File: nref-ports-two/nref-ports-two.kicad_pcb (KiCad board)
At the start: 4 copper layers, 87.5 x 40.2 mm, 117 parts, among them J1 USB_C_Receptacle, J2 USB_C_Receptacle, J3 USB3_A, J4 HD0919MSMTTR, J5 Conn_01x20, J6 Conn_01x12_Pin, J7 Conn_01x04, U1 TUSB8041, U10 TPD4E02B04DQA, U11 TPD12S521, U12 LM2830XQMFE/NOPB, U13 LM2830XQMFE/NOPB, U2 HD3SS3220IRNHT, U3 TPD4E02B04DQA, U4 TPD4E02B04DQA, U5 TPD4E02B04DQA, U6 TPD4E02B04DQA, U7 TPD4E02B04DQA, U8 TPD4E02B04DQA, U9 TPD4E02B04DQA, Y1 24MHz

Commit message: WIP ports-two redesign
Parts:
- removed D2, D3: PMEG1020EA,115, Diode_SMD:D_SOD-323
- removed FB1, FB2: 220@100MHz 1.4A, Inductor_SMD:L_0603_1608Metric
- removed J7: Conn_01x04, Connector_JST:JST_SH_SM04B-SRSS-TB_1x04-1MP_P1.00mm_Horizontal
- removed R39, R40, R43, R44: 22k, Resistor_SMD:R_0402_1005Metric
- added C44: 0.1uF, Capacitor_SMD:C_0402_1005Metric, F.Cu at (139.2, 97.3)
- added C45: 0.1uF, Capacitor_SMD:C_0402_1005Metric, F.Cu at (132.8, 99.2)
- added C46: 0.1uF, Capacitor_SMD:C_0402_1005Metric, F.Cu at (170.3, 110.0)
- added C47: 0.1uF, Capacitor_SMD:C_0402_1005Metric, F.Cu at (170.3, 109.0)
- added C48: 1uF, Capacitor_SMD:C_0402_1005Metric, F.Cu at (180.2, 104.3)
- added C49: 1uF, Capacitor_SMD:C_0402_1005Metric, F.Cu at (182.5, 104.3)
- added C50: 4.7uF, Capacitor_SMD:C_0402_1005Metric, F.Cu at (173.3, 110.1)
- added C51: 4.7uF, Capacitor_SMD:C_0402_1005Metric, F.Cu at (176.8, 103.8)
- added C52: 0.1uF, Capacitor_SMD:C_0402_1005Metric, F.Cu at (173.3, 112.0)
- added C53: 1uF, Capacitor_SMD:C_0402_1005Metric, F.Cu at (173.3, 111.0)
- added C54: 1uF, Capacitor_SMD:C_0402_1005Metric, F.Cu at (179.7, 106.0)
- added C55: 0.1uF, Capacitor_SMD:C_0402_1005Metric, F.Cu at (178.7, 106.0)
- added C56: 0.1uF, Capacitor_SMD:C_0402_1005Metric, F.Cu at (172.6, 103.8)
- added C57: 0.1uF, Capacitor_SMD:C_0402_1005Metric, F.Cu at (172.6, 102.9)
- added C58: 0.1uF, Capacitor_SMD:C_0402_1005Metric, F.Cu at (175.8, 111.2)
- added C59: 0.1uF, Capacitor_SMD:C_0402_1005Metric, F.Cu at (174.8, 111.2)
- added FB5: 100@100MHz 3A, Inductor_SMD:L_0402_1005Metric, F.Cu at (171.9, 111.0)
- added FB6: 100@100MHz 3A, Inductor_SMD:L_0402_1005Metric, F.Cu at (176.8, 102.8)
- added J8: Conn_01x12_Pin, Connector_FFC-FPC:Hirose_FH12-12S-0.5SH_1x12-1MP_P0.50mm_Horizontal, F.Cu at (149.7, 115.5)
- added R10: 0, Resistor_SMD:R_0402_1005Metric, F.Cu at (178.2, 104.0)
- added R19: 900k, Resistor_SMD:R_0402_1005Metric, F.Cu at (132.9, 104.3)
- added R20: 0, Resistor_SMD:R_0402_1005Metric, F.Cu at (172.2, 97.2)
- added TP3: TestPoint, TestPoint:TestPoint_Pad_D1.0mm, F.Cu at (129.6, 102.0)
- added TP4: TestPoint, TestPoint:TestPoint_Pad_D1.0mm, F.Cu at (181.5, 99.0)
- added TP5: TestPoint, TestPoint:TestPoint_Pad_D1.0mm, F.Cu at (185.9, 100.0)
- added TP6: TestPoint, TestPoint:TestPoint_Pad_D1.0mm, F.Cu at (185.2, 98.0)
- added TP7: TestPoint, TestPoint:TestPoint_Pad_D1.0mm, F.Cu at (129.6, 99.9)
- added U14: EQCO5X31C0-I_6NX, footprints:QFN50P400X400X100-21N-D, F.Cu at (175.1, 107.0)
- added U15: LP5907MFX-1.2, Package_TO_SOT_SMD:SOT-23-5, F.Cu at (181.3, 102.2)
- added U16: TUSB321, Package_DFN_QFN:Texas_X2QFN-12_1.6x1.6mm_P0.4mm, F.Cu at (183.6, 93.9)
- added U17: TMUXHS4212, footprints:Texas-VQFN20_2.5x4.5mm_RKS, F.Cu at (136.1, 95.7)
- added U18: TUSB321, Package_DFN_QFN:Texas_X2QFN-12_1.6x1.6mm_P0.4mm, F.Cu at (133.3, 101.1)
- C17: value 47uF -> 0.1uF; footprint Capacitor_SMD:C_1206_3216Metric -> Capacitor_SMD:C_0402_1005Metric
- J1, J2: footprint footprints:MOLEX_105450-0101 -> Connector_USB:USB_C_Receptacle_Molex_105450-0101
- J5: footprint Connector_FFC-FPC:Hirose_FH12-20S-0.5SH_1x20-1MP_P0.50mm_Horizontal -> footprints:AMPHENOL_SFV20R-2STE1HLF
- R11: value 10k -> 0
- R12: value 900k -> 10k
- R13, R22: value 200k -> 10k
- R14: value 0 -> 4.7k
- R15: value 0 -> 900k
- R18, R24: value 200k -> 0
- R23: value 200k -> 4.7k
- R31, R35, R36: value 100k -> 10k
- TP1, TP2: footprint TestPoint:TestPoint_Pad_1.0x1.0mm -> TestPoint:TestPoint_Pad_D1.0mm
- U12, U13: value LM2830XQMFE/NOPB -> TLV62569DBV
- U2: value HD3SS3220IRNHT -> TMUXHS4212; footprint footprints:QFN40P450X250X80-31N120X320 -> footprints:Texas-VQFN20_2.5x4.5mm_RKS
- moved TP2 65.5 mm to (193.4, 100.1)
- moved TP1 64.0 mm to (192.6, 89.8)
- moved R14 54.3 mm to (183.5, 97.0), turned to 0 degrees
- moved C17 53.6 mm to (179.9, 99.3), turned to 0 degrees
- moved R15 53.4 mm to (183.5, 98.0), turned to 0 degrees
- moved R13 53.2 mm to (183.5, 96.1), turned to 0 degrees
- moved R12 52.2 mm to (183.9, 102.5), turned to -90 degrees
- moved R21 49.7 mm to (185.5, 93.4)
- moved C18 48.4 mm to (183.1, 92.0), turned to 0 degrees
- moved U2 43.9 mm to (176.9, 97.1)
- moved R25 43.6 mm to (166.8, 117.8), turned to 180 degrees
- moved R24 41.4 mm to (164.6, 117.8), turned to 0 degrees
- moved C21 28.9 mm to (180.3, 94.0)
- moved C23 28.8 mm to (181.3, 94.0)
- moved C22 28.2 mm to (172.8, 94.0)
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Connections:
- net /USB3_1_SSTXCN renamed /USBH3_TXCN
- net /USB3_1_SSTXCP renamed /USBH3_TXCP
- net /USBH_1A_AC_TXN renamed /USBC2A_TXCN
- net /USBH_1A_AC_TXP renamed /USBC2A_TXCP
- net /USBH_1B_AC_TXN renamed /USBC2B_TXCN
- net /USBH_1B_AC_TXP renamed /USBC2B_TXCP
- net /USBH_2A_AC_TXN renamed /USBC1A_TXCN
- net /USBH_2A_AC_TXP renamed /USBC1A_TXCP
- net /USBH_2B_AC_TXN renamed /USBC1B_TXCN
- net /USBH_2B_AC_TXP renamed /USBC1B_TXCP
- net CC1 renamed USBC1_CC1
- net CC2 renamed USBC1_CC2
- C17 pad 1: MUX_5V -> /MUX_3V3
- C18 pad 1: MUX_3V3 -> +5V
- C21 pad 2: USBH_2A_TXN -> USBC1A_TXN
- C22 pad 2: USBH_2B_TXN -> USBC1B_TXN
- C23 pad 2: USBH_2A_TXP -> USBC1A_TXP
- C24 pad 2: USBH_2B_TXP -> USBC1B_TXP
- C27 pad 2: USBH_MUXA_TXN -> USBC2A_TXN
- C28 pad 2: USBH_MUXB_TXN -> USBC2B_TXN
- C29 pad 2: USBH_MUXA_TXP -> USBC2A_TXP
- C30 pad 2: USBH_MUXB_TXP -> USBC2B_TXP
- C34 pad 1: USBH_1A_TXN -> USBH3_TXN
- C36 pad 1: USBH_1A_TXP -> USBH3_TXP
- J1 pad A10: USBH_2B_RXN -> USBC1B_RXN
- J1 pad A11: USBH_2B_RXP -> USBC1B_RXP
- J1 pad A6: USBH_2_DP -> USBC1_DP
- J1 pad A7: USBH_2_DN -> USBC1_DN
- J1 pad B10: USBH_2A_RXN -> USBC1A_RXN
- J1 pad B11: USBH_2A_RXP -> USBC1A_RXP
- J1 pad B6: USBH_2_DP -> USBC1_DP
- J1 pad B7: USBH_2_DN -> USBC1_DN
- J2 pad A10: USBH_MUXB_RXN -> USBC2B_RXN
- J2 pad A11: USBH_MUXB_RXP -> USBC2B_RXP
- J2 pad A5: MUXCC1 -> USBC2_CC1
- J2 pad A6: USBH_1_DP -> USBC2_DP
- J2 pad A7: USBH_1_DN -> USBC2_DN
- J2 pad B10: USBH_MUXA_RXN -> USBC2A_RXN
- J2 pad B11: USBH_MUXA_RXP -> USBC2A_RXP
- J2 pad B5: MUXCC2 -> USBC2_CC2
- J2 pad B6: USBH_1_DP -> USBC2_DP
- J2 pad B7: USBH_1_DN -> USBC2_DN
- J3 pad 5: USBH_1A_RXN -> USBH3_RXN
- J3 pad 6: USBH_1A_RXP -> USBH3_RXP
- J5 pad 1: Net-(J5-Pin_1) -> HDMI_TX2P
- J5 pad 10: HDMI_CLKN -> HDMI_CLKP
- J5 pad 11: HDMI_CLKP -> HDMI_CLKN
- J5 pad 13: HDMI_TX0N -> GND
- J5 pad 14: HDMI_TX0P -> HDMI_CEC
- J5 pad 15: GND -> HDMI_SCL
- J5 pad 16: HDMI_TX1N -> HDMI_SDA
- J5 pad 17: HDMI_TX1P -> HDMI_HPD
- J5 pad 18: GND -> Net-(J5-Pin_18)
- J5 pad 19: HDMI_TX2N -> Net-(J5-Pin_18)
- J5 pad 2: Net-(J5-Pin_1) -> HDMI_TX2N
- J5 pad 20: HDMI_TX2P -> Net-(J5-Pin_18)
- J5 pad 3: Net-(J5-Pin_1) -> GND
- J5 pad 4: HDMI_HPD -> HDMI_TX1P
- J5 pad 5: HDMI_SCL -> HDMI_TX1N
- J5 pad 6: HDMI_SDA -> GND
- J5 pad 7: HDMI_CEC -> HDMI_TX0P
- J5 pad 8: GND -> HDMI_TX0N
- L1 pad 1: Net-(D2-K) -> Net-(U12-SW)
- L2 pad 1: Net-(D3-K) -> Net-(U13-SW)
- R1 pad 1: Net-(J5-Pin_1) -> Net-(J5-Pin_18)
- R11 pad 1: MUX_5V -> /MUX_3V3
- R11 pad 2: Net-(U2-CURRENT_MODE) -> +3V3
- R12 pad 1: MUX_5V -> Net-(U15-EN)
- R12 pad 2: Net-(U2-VBUS_DET) -> +3V3
- R13 pad 1: MUX_5V -> +5V
- R13 pad 2: Net-(U2-PORT) -> Net-(U16-CURRENT_MODE)
- R14 pad 1: MUXCC2 -> +5V
- R14 pad 2: Net-(U2-CC2) -> Net-(U16-PORT)
- R15 pad 1: MUXCC1 -> +5V
- R15 pad 2: Net-(U2-CC1) -> Net-(U16-VBUS_DET)
- R16 pad 1: GND -> /MUX_3V3
- R16 pad 2: Net-(U2-~{ENN_CC}) -> +3V3
- R17 pad 1: GND -> ~{USB_MUX_OE}
- R17 pad 2: Net-(U2-~{ENN_MUX}) -> Net-(U17-~{OE})
- R18 pad 1: Net-(U2-DIR) -> USBC2_MUX_DIR
- R18 pad 2: MUX_3V3 -> Net-(U17-SEL)
- R21 pad 1: MUX_3V3 -> USBC1_MUX_DIR
- R21 pad 2: +3V3 -> Net-(U2-SEL)
- R22 pad 1: Net-(U2-ID) -> +5V
- R22 pad 2: MUX_5V -> Net-(U18-CURRENT_MODE)
- R23 pad 1: Net-(U2-~{INT_N}/OUT3) -> +5V
- R23 pad 2: MUX_5V -> Net-(U18-PORT)
- R24 pad 1: Net-(U2-VCONN_FAULT_N) -> +3V3
- R24 pad 2: MUX_5V -> USBH_3V3
- R25 pad 1: MUX_5V -> +1V1
- R25 pad 2: +5V -> USBH_1V1
- TP1 pad 1: Net-(U2-SCL/OUT2) -> Net-(U16-ID)
- TP2 pad 1: Net-(U2-SDA/OUT1) -> Net-(U16-~{VCONN_FAULT})
- U1 pad 1: USBH_1_DP -> USBC1_DP
- U1 pad 10: USBH_2_DN -> USBH_3_DN
- U1 pad 11: USBH_2A_TXP -> USBH3_TXP
- U1 pad 12: USBH_2A_TXN -> USBH3_TXN
- U1 pad 14: USBH_2A_RXP -> USBH3_RXP
- U1 pad 15: USBH_2A_RXN -> USBH3_RXN
- U1 pad 17: USBH_3_DP -> USBC2_DP
- U1 pad 18: USBH_3_DN -> USBC2_DN
- U1 pad 19: USBH_2B_TXP -> USBH2_TXP
- U1 pad 2: USBH_1_DN -> USBC1_DN
- U1 pad 20: USBH_2B_TXN -> USBH2_TXN
- U1 pad 22: USBH_2B_RXN -> USBH2_RXP
- U1 pad 23: USBH_2B_RXP -> USBH2_RXN
- U1 pad 26: USBH_1B_TXP -> USBH4_TXN
- U1 pad 27: USBH_1B_TXN -> USBH4_TXP
- U1 pad 29: USBH_1B_RXN -> USBH4_RXN
- U1 pad 3: USBH_1A_TXP -> USBH1_TXP
- U1 pad 30: USBH_1B_RXP -> USBH4_RXP
- U1 pad 4: USBH_1A_TXN -> USBH1_TXN
- U1 pad 55: USB2_RXP -> /UP_SSTXP
- U1 pad 56: USB2_RXN -> /UP_SSTXN
- U1 pad 58: USB2_TXP -> USB2_RE_TXN
- U1 pad 59: USB2_TXN -> USB2_RE_TXP
- U1 pad 6: USBH_1A_RXP -> USBH1_RXP
- U1 pad 7: USBH_1A_RXN -> USBH1_RXN
- U1 pad 9: USBH_2_DP -> USBH_3_DP
- U12 pad 1: Net-(D2-K) -> Net-(U12-EN)
- U12 pad 3: Net-(U12-FB) -> Net-(U12-SW)
- U12 pad 4: Net-(U12-EN) -> +5V
- U12 pad 5: +5V -> Net-(U12-FB)
- U13 pad 1: Net-(D3-K) -> Net-(U13-EN)
- U13 pad 3: Net-(U13-FB) -> Net-(U13-SW)
- U13 pad 4: Net-(U13-EN) -> +5V
- U13 pad 5: +5V -> Net-(U13-FB)
- U2 pad 1: Net-(U2-CC2) -> unconnected-(U2-RSVD1-Pad1)
- U2 pad 10: USBH_1B_RXN -> unconnected-(U2-RSVD2-Pad10)
- U2 pad 11: Net-(U2-DIR) -> GND
- U2 pad 12: Net-(U2-~{ENN_MUX}) -> USBC1B_TXP
- U2 pad 13: GND -> USBC1B_TXN
- U2 pad 14: USBH_MUXA_RXN -> USBC1B_RXP
- U2 pad 15: USBH_MUXA_RXP -> USBC1B_RXN
- U2 pad 16: USBH_MUXA_TXN -> USBC1A_TXN
- U2 pad 17: USBH_MUXA_TXP -> USBC1A_TXP
- U2 pad 18: USBH_MUXB_RXN -> USBC1A_RXN
- U2 pad 19: USBH_MUXB_RXP -> USBC1A_RXP
- U2 pad 2: Net-(U2-CC1) -> Net-(U2-~{OE})
- U2 pad 20: USBH_MUXB_TXN -> GND
- U2 pad 3: Net-(U2-CURRENT_MODE) -> USBH1_RXN
- U2 pad 4: Net-(U2-PORT) -> USBH1_RXP
- U2 pad 5: Net-(U2-VBUS_DET) -> GND
- U2 pad 6: USBH_1B_TXP -> /MUX_3V3
- U2 pad 7: USBH_1B_TXN -> USBH1_TXN
- U2 pad 8: MUX_3V3 -> USBH1_TXP
- U2 pad 9: USBH_1B_RXP -> Net-(U2-SEL)
- U3 pad 4: USBH_2_DN -> USBC1_DN
- U3 pad 5: USBH_2_DP -> USBC1_DP
- U3 pad 6: USBH_2_DP -> USBC1_DP
- U3 pad 7: USBH_2_DN -> USBC1_DN
- U4 pad 1: USBH_2A_RXN -> USBC1A_RXN
- U4 pad 10: USBH_2A_RXN -> USBC1A_RXN
- U4 pad 2: USBH_2A_RXP -> USBC1A_RXP
- U4 pad 9: USBH_2A_RXP -> USBC1A_RXP
- U5 pad 1: USBH_2B_RXN -> USBC1B_RXN
- U5 pad 10: USBH_2B_RXN -> USBC1B_RXN
- U5 pad 2: USBH_2B_RXP -> USBC1B_RXP
- U5 pad 9: USBH_2B_RXP -> USBC1B_RXP
- U6 pad 1: MUXCC1 -> USBC2_CC1
- U6 pad 10: MUXCC1 -> USBC2_CC1
- U6 pad 2: MUXCC2 -> USBC2_CC2
- U6 pad 4: USBH_1_DN -> USBC2_DN
- U6 pad 5: USBH_1_DP -> USBC2_DP
- U6 pad 6: USBH_1_DP -> USBC2_DP
- U6 pad 7: USBH_1_DN -> USBC2_DN
- U6 pad 9: MUXCC2 -> USBC2_CC2
- U7 pad 1: USBH_MUXA_RXN -> USBC2A_RXN
- U7 pad 10: USBH_MUXA_RXN -> USBC2A_RXN
- U7 pad 2: USBH_MUXA_RXP -> USBC2A_RXP
- U7 pad 9: USBH_MUXA_RXP -> USBC2A_RXP
- U8 pad 1: USBH_MUXB_RXN -> USBC2B_RXN
- U8 pad 10: USBH_MUXB_RXN -> USBC2B_RXN
- U8 pad 2: USBH_MUXB_RXP -> USBC2B_RXP
- U8 pad 9: USBH_MUXB_RXP -> USBC2B_RXP
- U9 pad 1: USBH_3_DN -> USBH_3_DP
- U9 pad 10: USBH_3_DN -> USBH_3_DP
- U9 pad 2: USBH_3_DP -> USBH_3_DN
- U9 pad 4: USBH_1A_RXP -> USBH3_RXP
- U9 pad 5: USBH_1A_RXN -> USBH3_RXN
- U9 pad 6: USBH_1A_RXN -> USBH3_RXN
- U9 pad 7: USBH_1A_RXP -> USBH3_RXP
- U9 pad 9: USBH_3_DP -> USBH_3_DN
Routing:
- net +5V: track 256.6 -> 60.2 mm, vias 9 -> 3
- net USBH_1V1: track 113.2 -> 7.58 mm, vias 12 -> 1
- net GND: track 122.1 -> 25.6 mm, vias 90 -> 22
- net USBH_3V3: track 77.4 -> 10.6 mm, vias 5 -> 0
- net USBH_1_DP: track 63.9 -> 0.00 mm, vias 4 -> 0
- net USBH_1_DN: track 63.8 -> 0.00 mm, vias 2 -> 0
- net Net-(J4-CEC): track 58.8 -> 0.00 mm, vias 1 -> 0
- net USBH_2B_RXP: track 55.8 -> 0.00 mm, vias 2 -> 0
- net USBH_2B_RXN: track 54.9 -> 0.00 mm, vias 2 -> 0
- net USBH_2A_RXN: track 52.5 -> 0.00 mm, vias 4 -> 0
- net USBH_2A_RXP: track 51.2 -> 0.00 mm, vias 4 -> 0
- net Net-(J4-SCL): track 50.3 -> 0.00 mm, vias 1 -> 0
- net USBH_2_DN: track 49.4 -> 0.00 mm, vias 4 -> 0
- net /USBC1A_TXCN: track 48.6 -> 0.79 mm, vias 2 -> 0
- net /USBC1B_TXCN: track 47.8 -> 0.00 mm, vias 2 -> 0
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
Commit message: ports-two: more routing
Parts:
- moved R11 52.9 mm to (179.6, 100.0)
- moved C11 16.9 mm to (153.0, 109.9)
- moved C14 16.6 mm to (156.9, 100.0), turned to 90 degrees
- moved C13 16.1 mm to (167.1, 108.8), turned to 0 degrees
- moved R22 10.6 mm to (128.2, 101.8), turned to 90 degrees
- moved R23 10.2 mm to (129.2, 101.8), turned to 90 degrees
- moved TP2 8.37 mm to (186.1, 96.0)
- moved R18 7.10 mm to (130.2, 96.8)
- moved TP1 7.05 mm to (185.8, 91.8)
- moved R21 6.97 mm to (180.3, 98.1), turned to 180 degrees
- moved R24 5.63 mm to (159.0, 118.5), turned to 90 degrees
- moved C45 4.89 mm to (128.2, 97.3), turned to 180 degrees
- moved R16 4.70 mm to (132.4, 107.9), turned to -90 degrees
- moved R3 4.38 mm to (162.1, 116.8), turned to 180 degrees
- moved U18 4.11 mm to (129.6, 99.3)
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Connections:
- C17 pad 1: /MUX_3V3 -> Net-(U2-VCC)
- C44 pad 1: /MUX_3V3 -> Net-(U17-VCC)
- R11 pad 1: /MUX_3V3 -> Net-(U2-VCC)
- R16 pad 1: /MUX_3V3 -> Net-(U17-VCC)
- U17 pad 12: USBC2B_TXP -> USBC2A_TXP
- U17 pad 13: USBC2B_TXN -> USBC2A_TXN
- U17 pad 14: USBC2B_RXP -> USBC2A_RXP
- U17 pad 15: USBC2B_RXN -> USBC2A_RXN
- U17 pad 16: USBC2A_TXN -> USBC2B_TXN
- U17 pad 17: USBC2A_TXP -> USBC2B_TXP
- U17 pad 18: USBC2A_RXN -> USBC2B_RXN
- U17 pad 19: USBC2A_RXP -> USBC2B_RXP
- U17 pad 6: /MUX_3V3 -> Net-(U17-VCC)
- U2 pad 12: USBC1B_TXP -> USBC1A_TXP
- U2 pad 13: USBC1B_TXN -> USBC1A_TXN
- U2 pad 14: USBC1B_RXP -> USBC1A_RXP
- U2 pad 15: USBC1B_RXN -> USBC1A_RXN
- U2 pad 16: USBC1A_TXN -> USBC1B_TXN
- U2 pad 17: USBC1A_TXP -> USBC1B_TXP
- U2 pad 18: USBC1A_RXN -> USBC1B_RXN
- U2 pad 19: USBC1A_RXP -> USBC1B_RXP
- U2 pad 6: /MUX_3V3 -> Net-(U2-VCC)
- U5 pad 1: USBC1B_RXN -> /USBC1B_TXCN
- U5 pad 10: USBC1B_RXN -> /USBC1B_TXCN
- U5 pad 2: USBC1B_RXP -> /USBC1B_TXCP
- U5 pad 4: /USBC1B_TXCP -> USBC1B_RXN
- U5 pad 5: /USBC1B_TXCN -> USBC1B_RXP
- U5 pad 6: /USBC1B_TXCN -> USBC1B_RXP
- U5 pad 7: /USBC1B_TXCP -> USBC1B_RXN
- U5 pad 9: USBC1B_RXP -> /USBC1B_TXCP
- U8 pad 1: USBC2B_RXN -> /USBC2B_TXCN
- U8 pad 10: USBC2B_RXN -> /USBC2B_TXCN
- U8 pad 2: USBC2B_RXP -> /USBC2B_TXCP
- U8 pad 4: /USBC2B_TXCN -> USBC2B_RXN
- U8 pad 5: /USBC2B_TXCP -> USBC2B_RXP
- U8 pad 6: /USBC2B_TXCP -> USBC2B_RXP
- U8 pad 7: /USBC2B_TXCN -> USBC2B_RXN
- U8 pad 9: USBC2B_RXP -> /USBC2B_TXCP
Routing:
- net +5V: track 60.2 -> 158.3 mm, vias 3 -> 16
- net USBH_1V1: track 7.58 -> 58.2 mm, vias 1 -> 8
- net USBH_3V3: track 10.6 -> 53.7 mm, vias 0 -> 4
- net GND: track 25.6 -> 63.1 mm, vias 22 -> 78
- net USBC1_DN: track 1.37 -> 27.8 mm, vias 1 -> 4
- net USBC1_DP: track 1.08 -> 27.5 mm, vias 1 -> 2
- net USBC2_CC2: track 0.00 -> 18.7 mm, vias 0 -> 4
- net USBC2_CC1: track 0.00 -> 17.2 mm, vias 0 -> 4
- net USBC1_CC2: track 0.00 -> 15.0 mm, vias 0 -> 4
- net USBC1_CC1: track 0.00 -> 14.5 mm, vias 0 -> 4
- net USBC2_DN: track 19.7 -> 32.5 mm, vias 0 -> 4
- net USBC2_DP: track 19.2 -> 31.7 mm, vias 0 -> 2
- net USBC1A_RXP: track 0.00 -> 11.4 mm, vias 0 -> 2
- net USBC2A_RXP: track 0.00 -> 11.4 mm, vias 0 -> 2
- net USBC2A_RXN: track 0.00 -> 11.3 mm, vias 0 -> 2
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
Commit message: commit various notes / polishing for ports-one and ports-two
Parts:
- added R39: 0, Resistor_SMD:R_0402_1005Metric, F.Cu at (182.9, 94.7)
- added R40: 0, Resistor_SMD:R_0402_1005Metric, F.Cu at (127.2, 98.8)
- added R43: 0, Resistor_SMD:R_0402_1005Metric, F.Cu at (127.2, 99.8)
- R15, R19: value 900k -> 909k
- R17, R20: value 0 -> 10k
- moved H3 68.4 mm to (115.3, 114.8), turned to 0 degrees
- moved R1 65.3 mm to (182.9, 93.7)
- moved C37 19.5 mm to (108.1, 108.3), turned to 180 degrees
- moved C35 18.3 mm to (108.1, 106.5), turned to 0 degrees
- moved TP4 18.0 mm to (183.7, 117.6)
- moved TP6 16.7 mm to (184.8, 115.8)
- moved C38 16.2 mm to (108.7, 100.2), turned to -90 degrees
- moved TP5 16.2 mm to (182.7, 115.8)
- moved C33 6.13 mm to (108.2, 98.8), turned to 0 degrees
- moved R28 3.80 mm to (121.7, 101.0)
- moved R16 3.79 mm to (134.2, 104.5)
- moved R26 3.59 mm to (108.1, 107.4), turned to 0 degrees
- moved TP2 3.45 mm to (186.1, 99.5)
- moved R41 1.87 mm to (140.1, 114.2), turned to 180 degrees
- moved R15 1.16 mm to (186.1, 96.8)
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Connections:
- J5 pad 18: Net-(J5-Pin_18) -> +5V
- J5 pad 19: Net-(J5-Pin_18) -> +5V
- J5 pad 20: Net-(J5-Pin_18) -> +5V
- R1 pad 1: Net-(J5-Pin_18) -> USBC1_CC1
- R1 pad 2: +5V -> Net-(U16-CC1)
- R17 pad 1: ~{USB_MUX_OE} -> Net-(U17-~{OE})
- R17 pad 2: Net-(U17-~{OE}) -> GND
- R20 pad 1: ~{USB_MUX_OE} -> GND
- U16 pad 1: USBC1_CC1 -> Net-(U16-CC1)
- U16 pad 2: USBC1_CC2 -> Net-(U16-CC2)
- U18 pad 1: USBC2_CC1 -> Net-(U18-CC1)
- U18 pad 2: USBC2_CC2 -> Net-(U18-CC2)
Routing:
- net +5V: track 158.3 -> 290.7 mm, vias 16 -> 32
- net +3V3: track 89.8 -> 154.5 mm, vias 3 -> 9
- net Net-(J4-CEC): track 0.00 -> 20.3 mm
- net Net-(J4-+5V): track 0.00 -> 18.9 mm, vias 0 -> 2
- net Net-(J4-SCL): track 0.00 -> 15.4 mm, vias 0 -> 1
- net GND: track 63.1 -> 78.1 mm, vias 78 -> 244
- net Net-(U14-TSC): track 0.50 -> 14.9 mm, vias 1 -> 2
- net Net-(J4-HPD): track 0.00 -> 13.4 mm, vias 0 -> 2
- net Net-(J4-SDA): track 0.00 -> 12.8 mm, vias 0 -> 1
- net Net-(U14-LOM): track 0.00 -> 11.8 mm, vias 0 -> 2
- net Net-(U14-TSI): track 0.00 -> 10.7 mm, vias 0 -> 2
- net Net-(U17-VCC): track 1.07 -> 7.27 mm, vias 1 -> 2
- net HDMI_TX2P: track 28.7 -> 32.1 mm
- net Net-(U16-~{VCONN_FAULT}): track 1.92 -> 5.16 mm
- net Net-(U11-LV_SUPPLY): track 0.00 -> 3.15 mm
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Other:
- board text added: "HDMI"
- board text added: "Stackup: JLC04161H-3313 90 ohms coplanar diff pairs, w: 0.1547mm, s: 0.2mm"
- board text added: "USB▶CAM"
- board text added: "USB◀MB"

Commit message: PCBs: add various notes
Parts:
- added C60: 0.1uF, Capacitor_SMD:C_0402_1005Metric, F.Cu at (171.2, 61.1)
- added C61: 0.1uF, Capacitor_SMD:C_0402_1005Metric, F.Cu at (171.2, 63.1)
- added R44: 4.7k, Resistor_SMD:R_0402_1005Metric, F.Cu at (168.3, 61.1)
- added R45: 4.7k, Resistor_SMD:R_0402_1005Metric, F.Cu at (168.3, 63.1)
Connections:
- J8 pad 4: USBH4_TXN -> /USBH4_AC_TXN
- J8 pad 5: USBH4_TXP -> /USBH4_AC_TXP
- R1 pad 1: USBC1_CC1 -> USBC1_CC2
- R39 pad 1: USBC1_CC2 -> USBC1_CC1
- R40 pad 1: USBC2_CC1 -> USBC2_CC2
- R43 pad 1: USBC2_CC2 -> USBC2_CC1

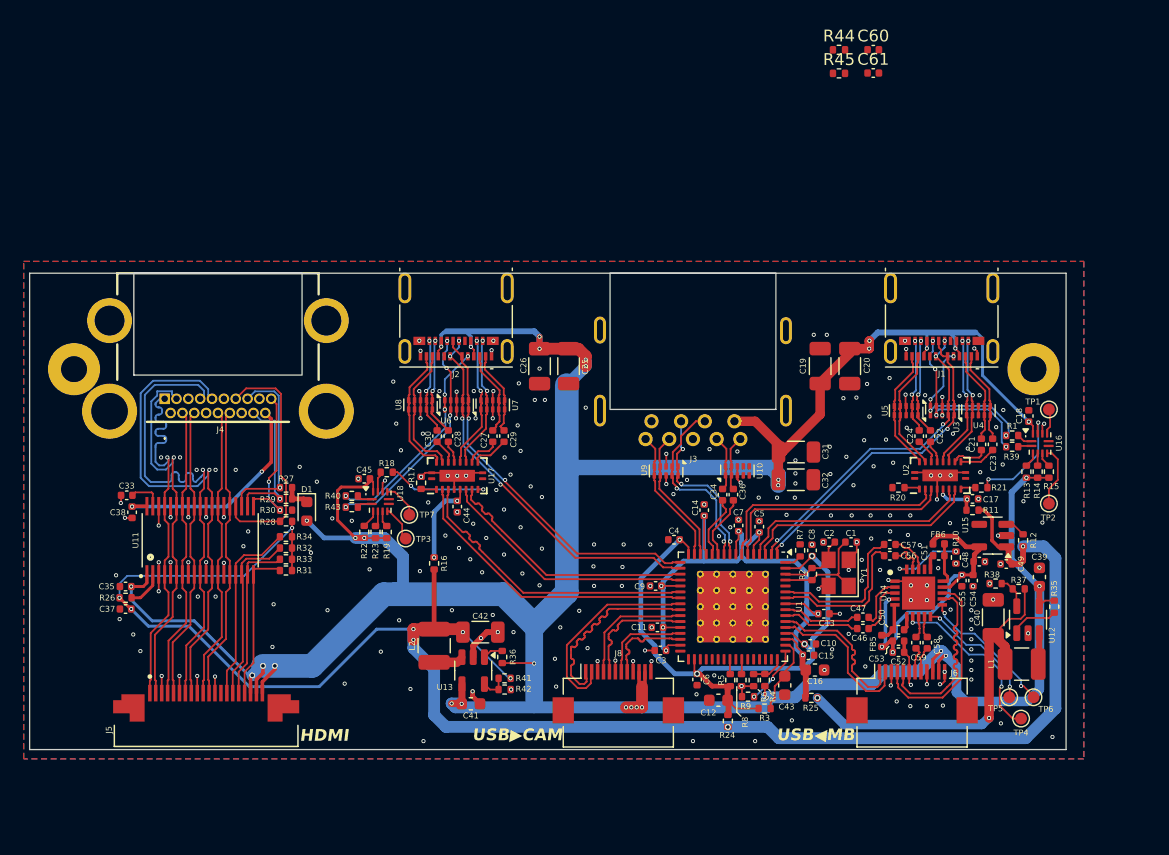
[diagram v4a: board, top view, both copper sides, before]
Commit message: ports-two: snapshot of r2 before switch to nxp redriver
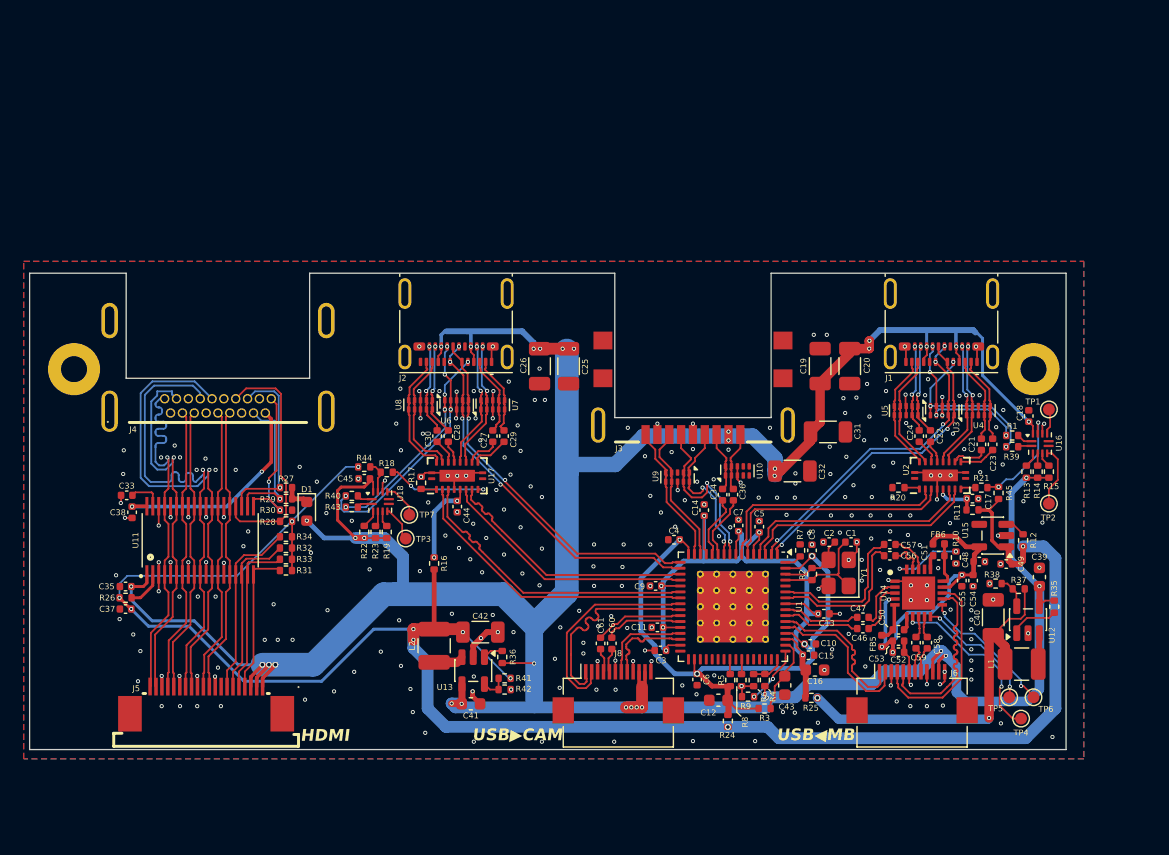
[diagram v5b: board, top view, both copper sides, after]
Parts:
- C21, C22, C23, C24, C27, C28, C29, C30, C34, C36, C46, C47, C56, C57, C58, C59, C60, C61: value 0.1uF -> 0.22uF
- J3: footprint footprints:WURTH_692121230100 -> footprints:USB-A-SMD_HC-USB3.0-C225-P
- J4: value HD0919MSMTTR -> A71-05H8-111N2; footprint footprints:HD0919MSMTTR -> footprints:HDMI-TH_A71-05H8-111N2
- J5: footprint footprints:AMPHENOL_SFV20R-2STE1HLF -> footprints:FPC-SMD_AFC07-S20ECC-00
- moved C60 54.8 mm to (149.2, 111.2), turned to 90 degrees
- moved C61 53.4 mm to (148.2, 111.2), turned to 90 degrees
- moved R44 53.3 mm to (128.2, 96.3)
- moved R45 37.9 mm to (181.8, 98.5), turned to 90 degrees
- moved J4 5.25 mm to (115.9, 87.9), turned to 180 degrees
- moved J3 4.35 mm to (156.0, 89.7)
- moved C31 3.19 mm to (167.4, 93.4)
- moved J5 1.81 mm to (114.9, 116.0)
- moved U9 1.09 mm to (154.7, 97.2)
- moved C32 0.79 mm to (164.4, 96.7)
- moved J1 0.47 mm to (177.0, 84.3)
- moved J2 0.47 mm to (136.0, 84.3)
- turned H3 to 180 degrees
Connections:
- J5 pad 1: HDMI_TX2P -> +5V
- J5 pad 10: HDMI_CLKP -> HDMI_CLKN
- J5 pad 11: HDMI_CLKN -> HDMI_CLKP
- J5 pad 13: GND -> HDMI_TX0N
- J5 pad 14: HDMI_CEC -> HDMI_TX0P
- J5 pad 15: HDMI_SCL -> GND
- J5 pad 16: HDMI_SDA -> HDMI_TX1N
- J5 pad 17: HDMI_HPD -> HDMI_TX1P
- J5 pad 18: +5V -> GND
- J5 pad 19: +5V -> HDMI_TX2N
- J5 pad 2: HDMI_TX2N -> +5V
- J5 pad 20: +5V -> HDMI_TX2P
- J5 pad 3: GND -> +5V
- J5 pad 4: HDMI_TX1P -> HDMI_HPD
- J5 pad 5: HDMI_TX1N -> HDMI_SDA
- J5 pad 6: GND -> HDMI_SCL
- J5 pad 7: HDMI_TX0P -> HDMI_CEC
- J5 pad 8: HDMI_TX0N -> GND
- U9 pad 1: USBH_3_DP -> USBH_3_DN
- U9 pad 10: USBH_3_DP -> USBH_3_DN
- U9 pad 2: USBH_3_DN -> USBH_3_DP
- U9 pad 9: USBH_3_DN -> USBH_3_DP
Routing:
- net +3V3: track 154.5 -> 163.4 mm, vias 9 -> 10
- net +5V: track 290.7 -> 281.9 mm, vias 32 -> 34
- net USBH4_TXP: track 10.3 -> 6.67 mm
- net USBH4_TXN: track 10.4 -> 7.51 mm
- net USBH_3_DN: track 16.2 -> 13.6 mm
- net /USBH4_AC_TXN: track 0.00 -> 2.00 mm
- net /USBH4_AC_TXP: track 0.00 -> 1.95 mm
- net GND: track 78.1 -> 79.7 mm, vias 244 -> 285
- net USBC1_CC2: track 15.1 -> 13.7 mm
- net USBC2_CC2: track 19.4 -> 20.7 mm
- net USBC2_MUX_DIR: track 1.75 -> 2.82 mm
- net USBH3_RXP: track 11.6 -> 12.4 mm
- net USBH3_RXN: track 11.6 -> 12.4 mm
- net USBC1_DP: track 27.7 -> 27.0 mm
- net USBH_4_DN: track 17.2 -> 17.9 mm
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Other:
- outline, holes or cut-outs redrawn
